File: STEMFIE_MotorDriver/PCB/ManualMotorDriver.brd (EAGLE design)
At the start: 16 x 33.5 mm, 16 parts, among them U1 STM32F030F4P6, U2 LP2985-33DBVR, U3 L9110SO8, X1 53048-05

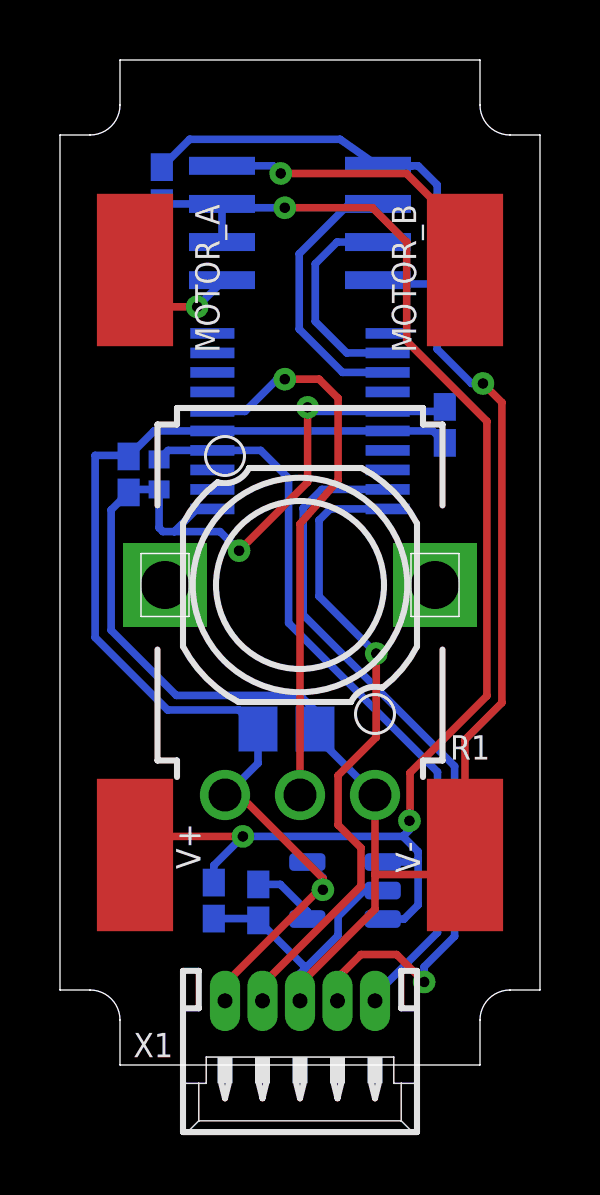
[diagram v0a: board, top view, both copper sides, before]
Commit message: Fix Potentiometer Center
Fixed slight potentiometer offset from center.
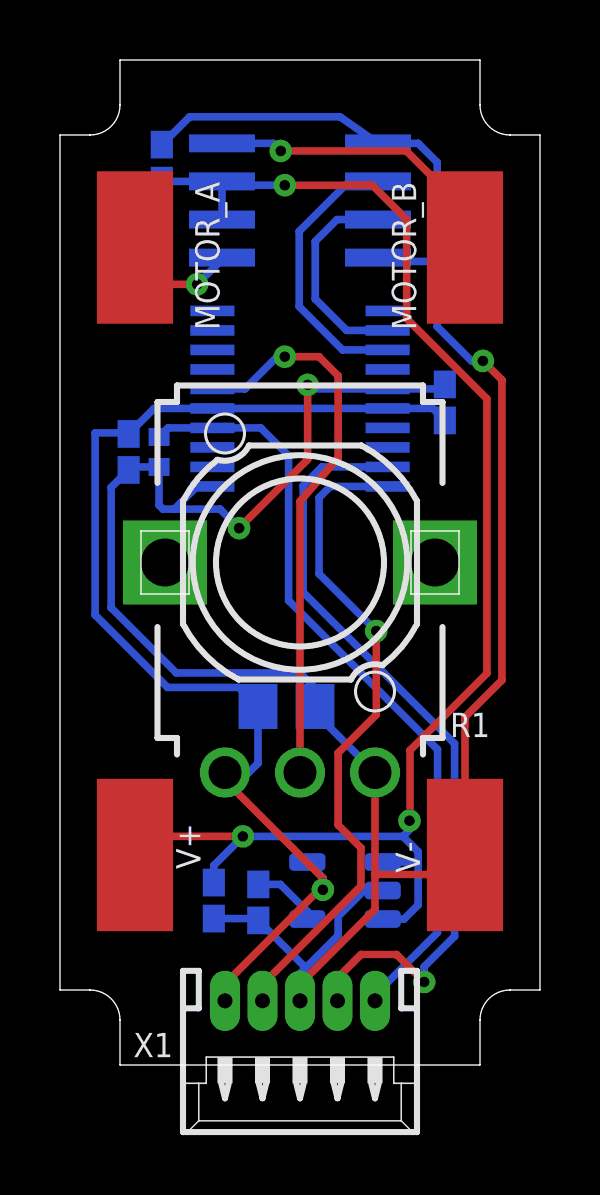
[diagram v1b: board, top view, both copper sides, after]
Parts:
- moved C2 0.75 mm to (12.8, 22.1)
- moved C3 0.75 mm to (2.29, 20.4)
- moved C4 0.75 mm to (3.39, 30.1)
- moved C6 0.75 mm to (7.55, 11.9)
- moved MOTOR_A 0.75 mm to (2.50, 27.2)
- moved MOTOR_B 0.75 mm to (13.5, 27.2)
- moved R1 0.75 mm to (8.00, 16.8)
- moved R2 0.75 mm to (3.30, 20.4)
- moved U1 0.75 mm to (8.00, 22.2)
- moved U3 0.75 mm to (8.00, 28.8)
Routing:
- net SWDIO: track 25.7 -> 26.5 mm
- net SWCLK: track 21.5 -> 22.2 mm
- net NRST: track 25.2 -> 25.9 mm
- net +5V: track 48.3 -> 49.0 mm
- net VCC: track 39.7 -> 40.4 mm

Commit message: Update Library
Created custom library for parts not in the standard Eagle libraries.
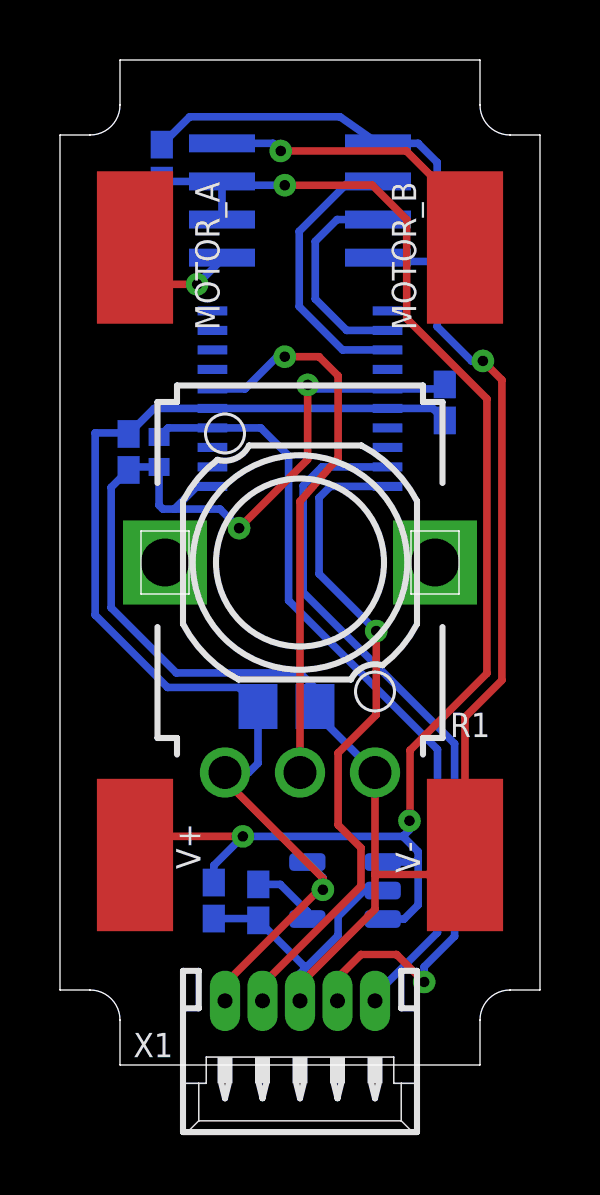
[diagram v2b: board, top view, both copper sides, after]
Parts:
- U1: device STM32:TSSOP20 -> STEMFIE_Electrics:TSSOP20
- turned U1 to 90 degrees
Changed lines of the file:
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@@
 </autorouter>
 <elements>
-<element name="U1" library="STM32" package="TSSOP20" value="STM32F030F4P6" x="8" y="22.211" smashed="yes" rot="MR180">
-<attribute name="COPYRIGHT" value="Copyright (C) 2022 Ultra Librarian. All rights reserved." x="34.67" y="38.721" size="1.778" layer="28" rot="MR180" display="off"/>
-<attribute name="MANUFACTURER_PART_NUMBER" value="STM32F030F4P6" x="34.67" y="38.721" size="1.778" layer="28" rot="MR180" display="off"/>
-<attribute name="MFR_NAME" value="STMicroelectronics" x="34.67" y="38.721" size="1.778" layer="28" rot="MR180" display="off"/>
-<attribute name="NAME" x="4.7234" y="22.846" size="1.27" layer="28" ratio="6" rot="SMR180"/>
-<attribute name="VALUE" x="6.2728" y="22.846" size="1.27" layer="28" ratio="6" rot="SMR180"/>
+<element name="U1" library="STEMFIE_Electrics" package="TSSOP20" package3d_urn="urn:adsk.eagle:package:4349/3" value="STM32F030F4P6" x="8" y="22.211" smashed="yes" rot="MR90">
+<attribute name="COPYRIGHT" value="Copyright (C) 2022 Ultra Librarian. All rights reserved." x="-8.51" y="48.881" size="1.778" layer="28" rot="MR90" display="off"/>
+<attribute name="MANUFACTURER_PART_NUMBER" value="STM32F030F4P6" x="-8.51" y="48.881" size="1.778" layer="28" rot="MR90" display="off"/>
+<attribute name="MFR_NAME" value="STMicroelectronics" x="-8.51" y="48.881" size="1.778" layer="28" rot="MR90" display="off"/>
+<attribute name="NAME" x="7.365" y="18.9344" size="1.27" layer="28" ratio="6" rot="SMR90"/>
+<attribute name="VALUE" x="7.365" y="20.4838" size="1.27" layer="28" ratio="6" rot="SMR90"/>
 </element>
 <element name="U2" library="LP2985-33DBVR" package="SOT95P280X145-5N" value="LP2985-33DBVR" x="9.5" y="5.815" smashed="yes" rot="MR0">
@@
 <wire x1="3.302" y1="19.935" x2="2.386" y2="19.935" width="0.254" layer="16"/>
 <wire x1="2.386" y1="19.935" x2="2.286" y2="19.835" width="0.254" layer="16"/>
-<wire x1="10.921" y1="22.536" x2="12.677" y2="22.536" width="0.254" layer="16"/>
+<wire x1="10.9178" y1="22.536" x2="12.677" y2="22.536" width="0.254" layer="16"/>
 <wire x1="12.677" y1="22.536" x2="12.827" y2="22.686" width="0.254" layer="16"/>
 <wire x1="10.6" y1="26.912" x2="10.347" y2="26.785" width="0.254" layer="16"/>
@@
 <wire x1="3.81" y1="18.53" x2="5.334" y2="18.53" width="0.254" layer="16"/>
 <wire x1="5.334" y1="18.53" x2="5.969" y2="17.895" width="0.254" layer="16"/>
-<wire x1="10.921" y1="22.536" x2="8.38960625" y2="22.536" width="0.254" layer="16"/>
+<wire x1="10.9178" y1="22.536" x2="8.38960625" y2="22.536" width="0.254" layer="16"/>
 <wire x1="8.38960625" y1="22.536" x2="8.255" y2="22.67060625" width="0.254" layer="16"/>
 <via x="8.255" y="22.67060625" extent="1-16" drill="0.35"/>
@@
 <wire x1="3.8767375" y1="13.069" x2="1.7048" y2="15.2409375" width="0.254" layer="16"/>
 <contactref element="U1" pad="1"/>
-<wire x1="5.079" y1="19.286" x2="4.566" y2="19.286" width="0.254" layer="16"/>
+<wire x1="5.0822" y1="19.286" x2="4.566" y2="19.286" width="0.254" layer="16"/>
 <wire x1="4.566" y1="19.286" x2="3.81" y2="18.53" width="0.254" layer="16"/>
 <wire x1="10.5" y1="6.35" x2="12.85" y2="6.35" width="0.254" layer="1"/>
@@
 <contactref element="C3" pad="1"/>
 <wire x1="3.137" y1="21.886" x2="2.286" y2="21.035" width="0.254" layer="16"/>
-<wire x1="3.137" y1="21.886" x2="5.079" y2="21.886" width="0.254" layer="16"/>
-<wire x1="10.921" y1="21.886003125" x2="12.426996875" y2="21.886003125" width="0.254" layer="16"/>
+<wire x1="3.137" y1="21.886" x2="5.0822" y2="21.886" width="0.254" layer="16"/>
+<wire x1="10.9178" y1="21.886" x2="12.426996875" y2="21.886003125" width="0.254" layer="16"/>
 <wire x1="12.426996875" y1="21.886003125" x2="12.827" y2="21.486" width="0.254" layer="16"/>
-<wire x1="5.079" y1="21.886" x2="4.697003125" y2="21.886003125" width="0.254" layer="16"/>
-<wire x1="4.697003125" y1="21.886003125" x2="10.921" y2="21.886003125" width="0.254" layer="16"/>
+<wire x1="5.0822" y1="21.886" x2="4.697003125" y2="21.886003125" width="0.254" layer="16"/>
+<wire x1="4.697003125" y1="21.886003125" x2="10.9178" y2="21.886" width="0.254" layer="16"/>
 <wire x1="2.286" y1="21.035" x2="2.251" y2="21.07" width="0.254" layer="16"/>
 <wire x1="2.251" y1="21.07" x2="1.1714" y2="21.07" width="0.254" layer="16"/>
@@
 <contactref element="X1" pad="2"/>
 <wire x1="8.636" y1="18.911" x2="9.011003125" y2="19.286003125" width="0.254" layer="16"/>
-<wire x1="9.011003125" y1="19.286003125" x2="10.921" y2="19.286003125" width="0.254" layer="16"/>
+<wire x1="9.011003125" y1="19.286003125" x2="10.9178" y2="19.286" width="0.254" layer="16"/>
 <wire x1="6.75" y1="2.686" x2="6.75" y2="2.139" width="0.254" layer="1"/>
 <wire x1="10.541" y1="11.672" x2="10.541" y2="14.466" width="0.254" layer="1"/>
@@
 <wire x1="8.1054" y1="15.7586" x2="8.1054" y2="19.3103875" width="0.254" layer="16"/>
 <wire x1="8.1054" y1="19.3103875" x2="8.7310125" y2="19.936" width="0.254" layer="16"/>
-<wire x1="8.7310125" y1="19.936" x2="10.921" y2="19.936" width="0.254" layer="16"/>
+<wire x1="8.7310125" y1="19.936" x2="10.9178" y2="19.936" width="0.254" layer="16"/>
 <wire x1="9.25" y1="2.139" x2="9.25" y2="2.9" width="0.254" layer="1"/>
 <wire x1="9.25" y1="2.9" x2="10.033" y2="3.683" width="0.254" layer="1"/>
@@
 <wire x1="7.493" y1="23.61" x2="7.239" y2="23.61" width="0.254" layer="16"/>
 <wire x1="6.164996875" y1="22.535996875" x2="7.239" y2="23.61" width="0.254" layer="16"/>
-<wire x1="6.164996875" y1="22.535996875" x2="5.079" y2="22.535996875" width="0.254" layer="16"/>
+<wire x1="6.164996875" y1="22.535996875" x2="5.0822" y2="22.536" width="0.254" layer="16"/>
 <wire x1="9.271" y1="20.23524375" x2="9.271" y2="22.975" width="0.254" layer="1"/>
 </signal>
@@
 <contactref element="X1" pad="5"/>
 <wire x1="3.302" y1="20.935" x2="3.603" y2="21.236" width="0.254" layer="16"/>
-<wire x1="3.603" y1="21.236" x2="5.079" y2="21.236" width="0.254" layer="16"/>
+<wire x1="3.603" y1="21.236" x2="5.0822" y2="21.236" width="0.254" layer="16"/>
 <wire x1="12.584" y1="4.414315625" x2="12.584" y2="10.518" width="0.254" layer="16"/>
 <wire x1="7.62" y1="15.482" x2="7.62" y2="20.308" width="0.254" layer="16"/>
 <wire x1="7.62" y1="20.308" x2="6.692" y2="21.236" width="0.254" layer="16"/>
-<wire x1="6.692" y1="21.236" x2="5.079" y2="21.236" width="0.254" layer="16"/>
+<wire x1="6.692" y1="21.236" x2="5.0822" y2="21.236" width="0.254" layer="16"/>
 <wire x1="12.584" y1="10.518" x2="7.62" y2="15.482" width="0.254" layer="16"/>
 <wire x1="10.5" y1="2.139" x2="10.5" y2="2.330315625" width="0.254" layer="16"/>
@@
 <contactref element="U3" pad="6"/>
 <contactref element="U1" pad="13"/>
-<wire x1="10.921" y1="23.836" x2="9.418" y2="23.836" width="0.254" layer="16"/>
+<wire x1="10.9178" y1="23.836" x2="9.418" y2="23.836" width="0.254" layer="16"/>
 <wire x1="9.418" y1="23.836" x2="7.974" y2="25.28" width="0.254" layer="16"/>
 <wire x1="7.974" y1="25.28" x2="7.974" y2="27.79" width="0.254" layer="16"/>
@@
 <wire x1="10.6" y1="28.182" x2="9.236" y2="28.182" width="0.254" layer="16"/>
 <wire x1="9.236" y1="28.182" x2="8.509" y2="27.455" width="0.254" layer="16"/>
-<wire x1="9.556996875" y1="24.486003125" x2="10.921" y2="24.486003125" width="0.254" layer="16"/>
+<wire x1="9.556996875" y1="24.486003125" x2="10.9178" y2="24.486" width="0.254" layer="16"/>
 <wire x1="8.509" y1="27.455" x2="8.509" y2="25.534" width="0.254" layer="16"/>
 <wire x1="8.509" y1="25.534" x2="9.556996875" y2="24.486003125" width="0.254" layer="16"/>

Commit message: Fixed NRST
nRST was pulled down instead of up. Yeah ...
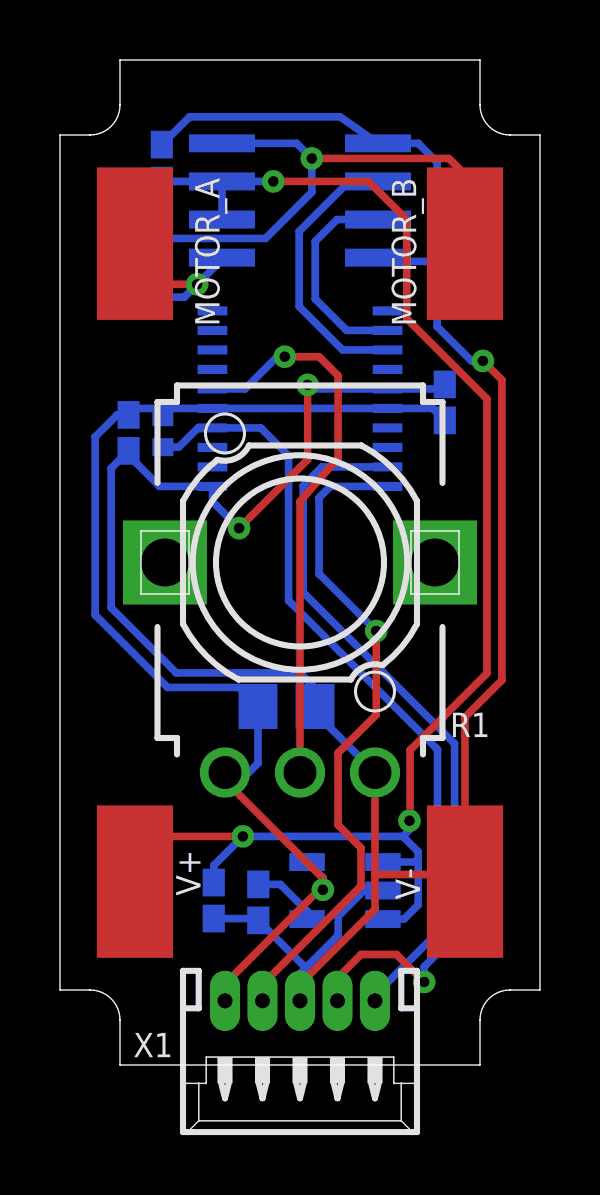
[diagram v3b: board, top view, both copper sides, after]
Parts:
- added C7: 100pF, rcl:C0805
- R1: value EVUF3L -> 10K
- R2: value (none) -> 10K
- U2: device LP2985-33DBVR:SOT95P280X145-5N -> STEMFIE_Electrics:SOT95P280X145-5N
- U3: device L9110:SO-08 -> STEMFIE_Electrics:SO-08
- moved V+ 0.89 mm to (2.50, 6.11)
- moved V- 0.89 mm to (13.5, 6.11)
- moved R2 0.67 mm to (3.43, 21.1), turned to 270 degrees
- moved C3 0.64 mm to (2.29, 21.1)
- moved MOTOR_A 0.13 mm to (2.50, 27.4)
- moved MOTOR_B 0.13 mm to (13.5, 27.4)
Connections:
- net GND: no longer R2.1
- net N$4: now also C7.1
- net N$5: now also C7.2
- net VCC: now also R2.1
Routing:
- net N$5: track 10.3 -> 19.0 mm
- net N$4: track 4.49 -> 6.95 mm
- net +5V: track 49.0 -> 49.9 mm

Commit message: Added LEDs and reduced size of wire pads
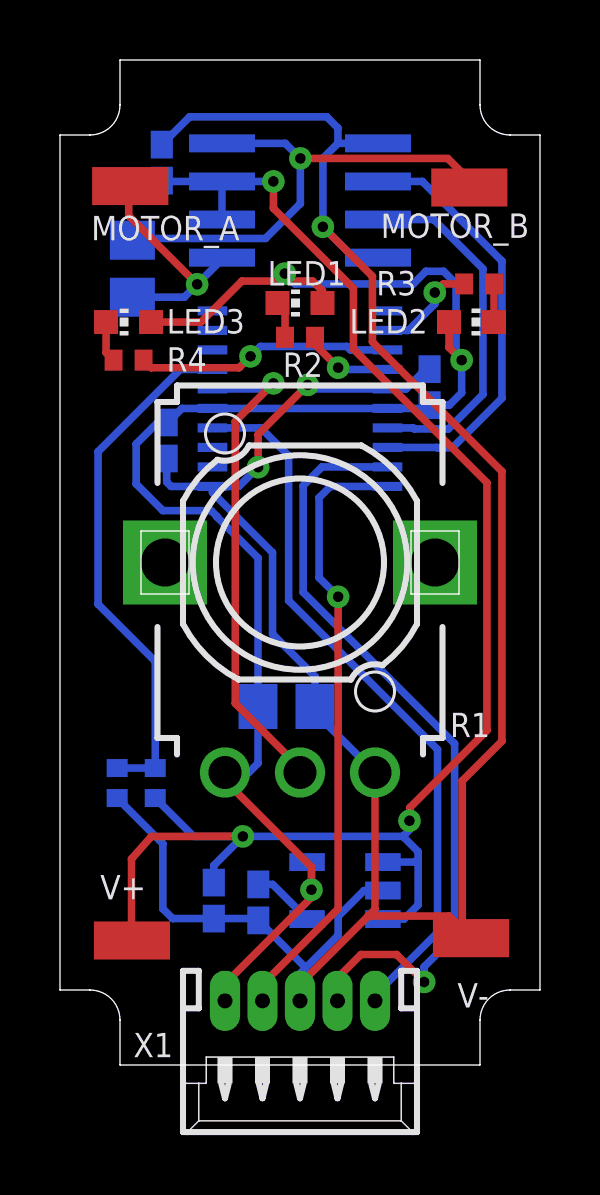
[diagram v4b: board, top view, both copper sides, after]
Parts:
- added LED1, LED2, LED3: (no value), led:CHIP-LED0603
- added R3, R4: 120R, rcl:R0402
- added R5: 2.2K, rcl:R0402
- added R6: 8K, rcl:R0402
- C3: value 1uF -> 10nF
- C6: value 2.2uF -> 4.7uF
- C7: value 100pF -> 10nF
- MOTOR_A, MOTOR_B, V+, V-: value (none) -> WIREPADSMD1,27-254; device wirepad:SMD2,54-5,08 -> wirepad:SMD1,27-2,54
- R2: value 10K -> 120R
- moved R2 5.56 mm to (8.00, 24.3), flipped to the top, turned to 180 degrees
- moved V+ 1.96 mm to (2.40, 4.15), turned to 90 degrees
- moved MOTOR_A 1.93 mm to (2.34, 29.3), turned to 90 degrees
- moved V- 1.89 mm to (13.7, 4.23), turned to 90 degrees
- moved MOTOR_B 1.88 mm to (13.6, 29.2), turned to 90 degrees
- moved C3 1.30 mm to (3.56, 20.8)
- moved C2 0.72 mm to (12.3, 22.6)
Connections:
- new net LED_CCW: R4.1, U1.13
- new net LED_CW: R3.1, U1.12
- new net LED_PWR: R2.1, U1.14
- new net N$2: LED1.C, R2.2
- new net N$6: LED2.C, R3.2
- new net N$7: LED3.C, R4.2
- new net V_IN: R5.2, R6.1, U1.7
- net +5V: now also R6.2
- net GND: now also R5.1
- net MOTOR_A: now also U1.18; no longer U1.13
- net MOTOR_B: now also U1.17; no longer U1.12
- net NRST: no longer R2.2
- net VCC: now also LED1.A, LED2.A, LED3.A; no longer R2.1
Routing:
- net V_IN: track 0.00 -> 17.6 mm
- net VCC: track 40.7 -> 55.9 mm, vias 1 -> 3
- net LED_CCW: track 0.00 -> 8.58 mm, vias 0 -> 1
- net MOTOR_A: track 9.37 -> 14.3 mm
- net MOTOR_B: track 7.16 -> 12.0 mm
- net +5V: track 49.9 -> 53.5 mm
- net LED_CW: track 0.00 -> 3.42 mm, vias 0 -> 1
- net LED_PWR: track 0.00 -> 3.00 mm, vias 0 -> 1
- net N$5: track 19.0 -> 16.6 mm
- net N$1: track 18.6 -> 16.5 mm
- net NRST: track 25.9 -> 24.0 mm
- net SWCLK: track 22.2 -> 20.5 mm
- net N$7: track 0.00 -> 1.37 mm
- net N$6: track 0.00 -> 1.27 mm
- net N$2: track 0.00 -> 1.25 mm
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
